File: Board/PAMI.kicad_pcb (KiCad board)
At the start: 4 copper layers, 28.6 x 38.2 mm, 48 parts, among them J1 Conn_01x04_Pin, SW1 Conn_01x03_Pin, U1 BD9P135MUF-CE2, U2 STM32L031F6Px, U3 TC78H621FNG

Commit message: Fix some minor glith on plan & add logo
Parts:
- added G***: LOGO, PAMI:krabi, F.Cu at (71.0, 94.0)

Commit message: Fix DCR
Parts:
- moved SW1 0.31 mm to (84.2, 68.7)
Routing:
- net 9V: track 33.7 -> 33.1 mm

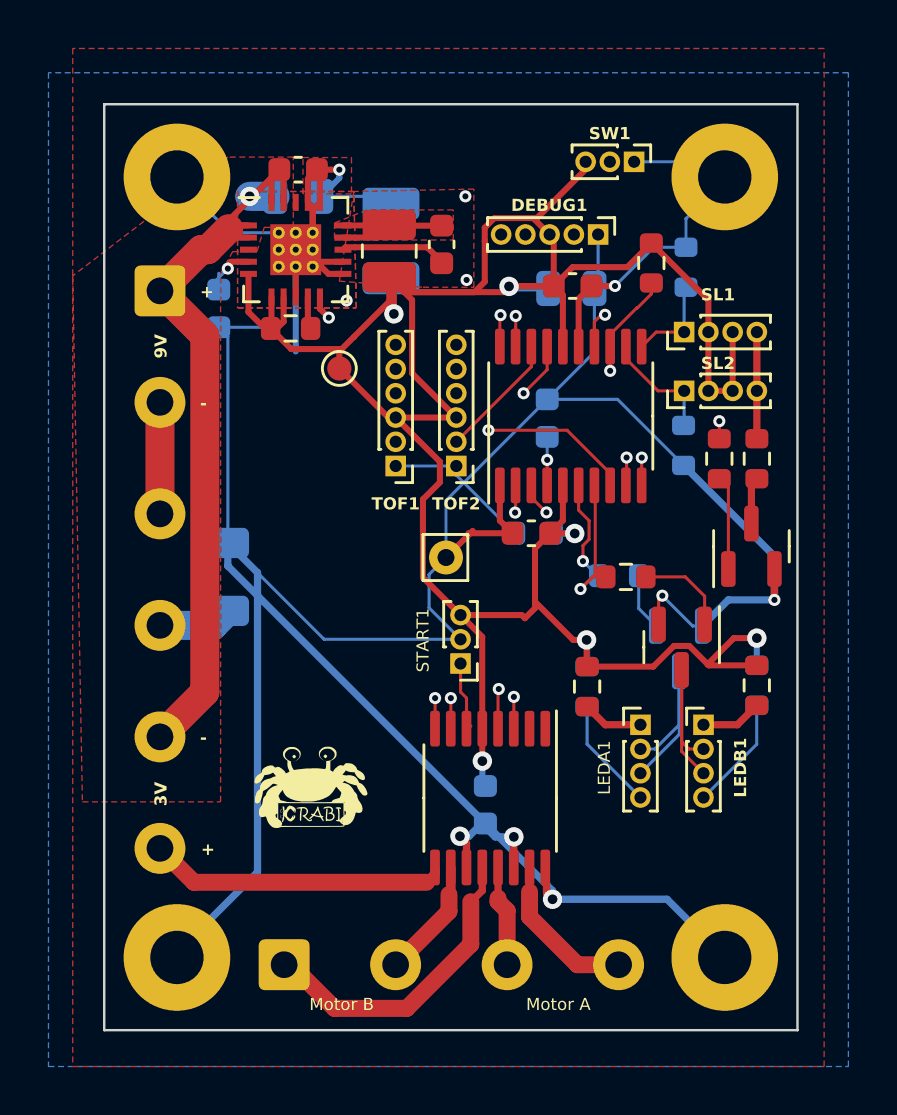
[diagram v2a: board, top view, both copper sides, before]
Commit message: review (fix warnings + GND copper fill on internal layers)
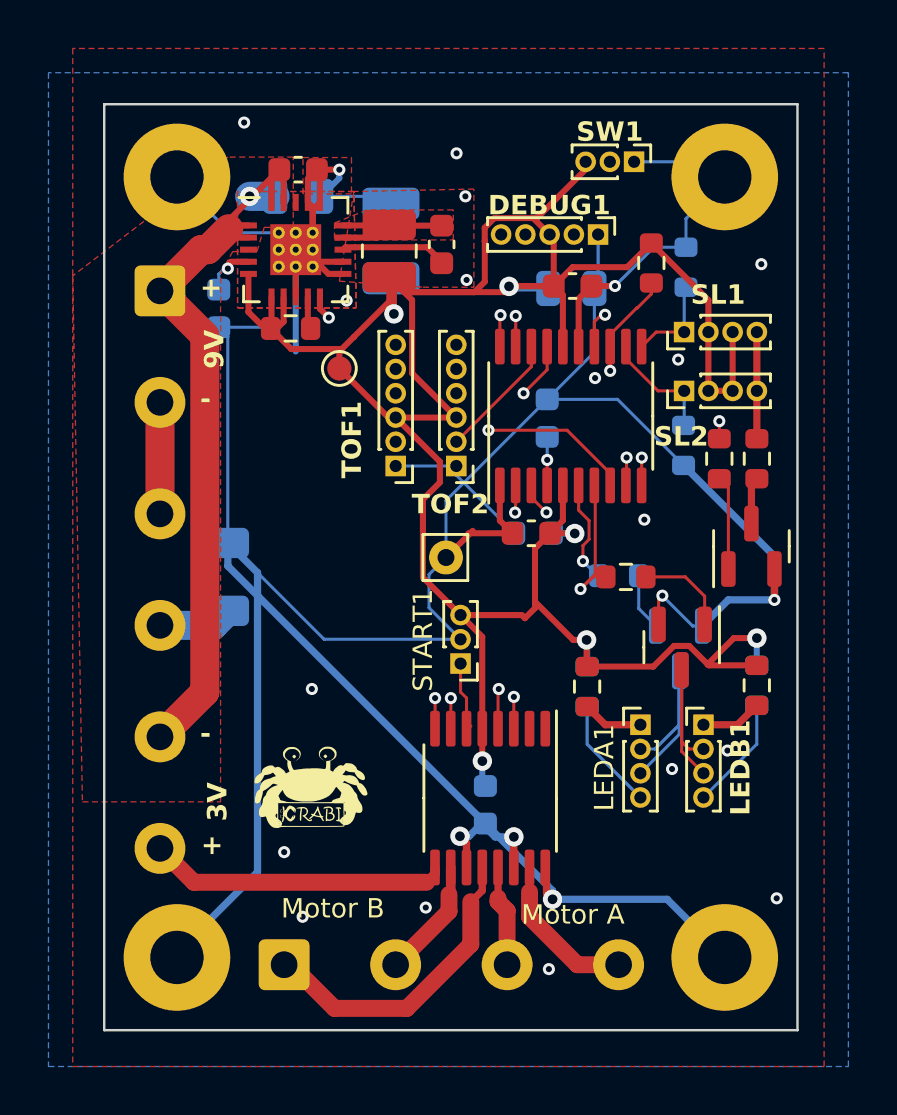
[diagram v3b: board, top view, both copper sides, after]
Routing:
- net GND: vias 10 -> 24
- added copper zone on In1.Cu, net GND
- added copper zone on In2.Cu, net GND
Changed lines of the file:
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@@
     (attr through_hole)
     (fp_text reference "LEDA1" (at -1.491564 1.769999 90) (layer "F.SilkS")
-        (effects (font (size 0.5 0.5) (thickness 0.1)))
+        (effects (font (size 0.8 0.8) (thickness 0.1)))
     )
     (fp_text value "Conn_01x04_Pin" (at -2.9 4.56) (layer "F.Fab")
@@
     (property "ki_keywords" "connector")
     (attr through_hole)
-    (fp_text reference "TOF1" (at 0 -1.56) (layer "F.SilkS")
-        (effects (font (size 0.5 0.5) (thickness 0.1) bold))
+    (fp_text reference "TOF1" (at 1.808 1.088 90) (layer "F.SilkS")
+        (effects (font (size 0.8 0.8) (thickness 0.1) bold))
     )
     (fp_text value "Conn_01x05_Pin" (at -0.1 6.381564) (layer "F.Fab")
@@
     (property "ki_keywords" "connector")
     (attr through_hole)
-    (fp_text reference "SL2" (at 1.135 1.395 180) (layer "F.SilkS")
-        (effects (font (size 0.5 0.5) (thickness 0.1) bold))
+    (fp_text reference "SL2" (at -1.885 -0.119 180) (layer "F.SilkS")
+        (effects (font (size 0.8 0.8) (thickness 0.1) bold))
     )
     (fp_text value "Conn_01x04_Pin" (at 0 4.56 90) (layer "F.Fab")
@@
     (attr through_hole)
     (fp_text reference "START1" (at 1.55 0.965 270) (layer "F.SilkS")
-        (effects (font (size 0.5 0.5) (thickness 0.1)))
+        (effects (font (size 0.8 0.8) (thickness 0.1)))
     )
     (fp_text value "Conn_01x03_Pin" (at 0 3.56) (layer "F.Fab")
@@
     (attr through_hole)
     (fp_text reference "SL1" (at 1.54 1.395) (layer "F.SilkS")
-        (effects (font (size 0.5 0.5) (thickness 0.1) bold))
+        (effects (font (size 0.8 0.8) (thickness 0.1) bold))
     )
     (fp_text value "Conn_01x04_Pin" (at 0 4.56 90) (layer "F.Fab")
@@
     (property "ki_keywords" "connector")
     (attr through_hole)
-    (fp_text reference "SW1" (at -1.165 1.005) (layer "F.SilkS")
-        (effects (font (size 0.5 0.5) (thickness 0.1) bold))
+    (fp_text reference "SW1" (at -1.238 1.005) (layer "F.SilkS")
+        (effects (font (size 0.8 0.8) (thickness 0.1) bold))
     )
     (fp_text value "Conn_01x03_Pin" (at 0 3.56 90) (layer "F.Fab")
@@
     (at 71 94)
     (attr board_only exclude_from_pos_files exclude_from_bom)
-    (fp_text reference "G***" (at -0.4 -2.3) (layer "F.Fab")
+    (fp_text reference "G***" (at -0.4 -2.3) (layer "F.Fab") hide
         (effects (font (size 1.5 1.5) (thickness 0.3)))
     )
@@
     (attr through_hole)
     (fp_text reference "LEDB1" (at 1.528436 1.77 90) (layer "F.SilkS")
-        (effects (font (size 0.5 0.5) (thickness 0.1) bold))
+        (effects (font (size 0.8 0.8) (thickness 0.1) bold))
     )
     (fp_text value "Conn_01x04_Pin" (at 0 4.56) (layer "F.Fab")
@@
     (property "ki_keywords" "connector")
     (attr through_hole)
-    (fp_text reference "TOF2" (at 0 -1.56) (layer "F.SilkS")
-        (effects (font (size 0.5 0.5) (thickness 0.1) bold))
+    (fp_text reference "TOF2" (at 0.244 -1.579) (layer "F.SilkS")
+        (effects (font (size 0.8 0.8) (thickness 0.1) bold))
     )
     (fp_text value "Conn_01x05_Pin" (at -5.425 6.581564) (layer "F.Fab")
@@
     (attr through_hole)
     (fp_text reference "DEBUG1" (at -1.205 2.015) (layer "F.SilkS")
-        (effects (font (size 0.5 0.5) (thickness 0.1) bold))
+        (effects (font (size 0.8 0.8) (thickness 0.1) bold))
     )
     (fp_text value "Conn_01x05_Pin" (at -0.3 7.16 90) (layer "F.Fab")
@@
   (gr_rect (start 62.3 66.3) (end 90.9 104.5)
     (stroke (width 0.1) (type default)) (fill none) (layer "Edge.Cuts"))
-  (gr_text "3V" (at 64.932 95.26 90) (layer "F.SilkS")
-    (effects (font (size 0.5 0.5) (thickness 0.1) bold) (justify left bottom))
+  (gr_text "3V" (at 67.437 95.885 90) (layer "F.SilkS")
+    (effects (font (size 0.8 0.8) (thickness 0.1) bold) (justify left bottom))
   )
   (gr_text "+" (at 66.25 74.332) (layer "F.SilkS")
-    (effects (font (size 0.5 0.5) (thickness 0.1) bold) (justify left bottom))
+    (effects (font (size 0.8 0.8) (thickness 0.1) bold) (justify left bottom))
   )
-  (gr_text "Motor B" (at 70.76 103.73) (layer "F.SilkS")
-    (effects (font (size 0.5 0.5) (thickness 0.1)) (justify left bottom))
+  (gr_text "Motor B" (at 69.596 99.949) (layer "F.SilkS")
+    (effects (font (size 0.8 0.8) (thickness 0.1)) (justify left bottom))
   )
   (gr_text "-" (at 66.25 92.732) (layer "F.SilkS")
-    (effects (font (size 0.5 0.5) (thickness 0.1) bold) (justify left bottom))
+    (effects (font (size 0.8 0.8) (thickness 0.1) bold) (justify left bottom))
   )
   (gr_text "-" (at 66.25 78.932) (layer "F.SilkS")
-    (effects (font (size 0.5 0.5) (thickness 0.1) bold) (justify left bottom))
+    (effects (font (size 0.8 0.8) (thickness 0.1) bold) (justify left bottom))
   )
-  (gr_text "Motor A" (at 79.7 103.73) (layer "F.SilkS")
-    (effects (font (size 0.5 0.5) (thickness 0.1)) (justify left bottom))
+  (gr_text "Motor A" (at 79.502 100.203) (layer "F.SilkS")
+    (effects (font (size 0.8 0.8) (thickness 0.1)) (justify left bottom))
   )
-  (gr_text "9V" (at 64.932 76.79 90) (layer "F.SilkS")
-    (effects (font (size 0.5 0.5) (thickness 0.1) bold) (justify left bottom))
+  (gr_text "9V" (at 67.31 77.216 90) (layer "F.SilkS")
+    (effects (font (size 0.8 0.8) (thickness 0.1) bold) (justify left bottom))
   )
   (gr_text "+" (at 66.29 97.332) (layer "F.SilkS")
-    (effects (font (size 0.5 0.5) (thickness 0.1) bold) (justify left bottom))
+    (effects (font (size 0.8 0.8) (thickness 0.1) bold) (justify left bottom))
   )
   (segment (start 79.146564 84) (end 77.321564 84) (width 0.25) (layer "F.Cu") (net 1))
@@
   (via (at 72.3 74.4) (size 0.5) (drill 0.25) (layers "F.Cu" "B.Cu") (free) (net 1))
   (via (at 80.796064 99.1) (size 0.8) (drill 0.4) (layers "F.Cu" "B.Cu") (net 1))
+  (via (at 75.565 99.441) (size 0.5) (drill 0.25) (layers "F.Cu" "B.Cu") (free) (net 1))
+  (via (at 70.485 99.822) (size 0.5) (drill 0.25) (layers "F.Cu" "B.Cu") (free) (net 1))
+  (via (at 88.011 92.964) (size 0.5) (drill 0.25) (layers "F.Cu" "B.Cu") (free) (net 1))
+  (via (at 89.408 72.898) (size 0.5) (drill 0.25) (layers "F.Cu" "B.Cu") (free) (net 1))
+  (via (at 76.835 68.326) (size 0.5) (drill 0.25) (layers "F.Cu" "B.Cu") (free) (net 1))
   (via (at 79.2 96.525) (size 0.8) (drill 0.4) (layers "F.Cu" "B.Cu") (net 1))
   (via (at 85.325 86.575) (size 0.5) (drill 0.25) (layers "F.Cu" "B.Cu") (net 1))
@@
   (via (at 83.371564 73.8) (size 0.5) (drill 0.25) (layers "F.Cu" "B.Cu") (net 1))
   (via (at 72 69) (size 0.5) (drill 0.25) (layers "F.Cu" "B.Cu") (net 1))
+  (via (at 85.979 76.835) (size 0.5) (drill 0.25) (layers "F.Cu" "B.Cu") (free) (net 1))
+  (via (at 82.55 77.597) (size 0.5) (drill 0.25) (layers "F.Cu" "B.Cu") (free) (net 1))
+  (via (at 70.866 90.424) (size 0.5) (drill 0.25) (layers "F.Cu" "B.Cu") (free) (net 1))
   (via (at 89.95 86.75) (size 0.5) (drill 0.25) (layers "F.Cu" "B.Cu") (net 1))
   (via (at 77.25 73.55) (size 0.5) (drill 0.25) (layers "F.Cu" "B.Cu") (free) (net 1))
+  (via (at 90.043 99.06) (size 0.5) (drill 0.25) (layers "F.Cu" "B.Cu") (free) (net 1))
+  (via (at 68.072 67.056) (size 0.5) (drill 0.25) (layers "F.Cu" "B.Cu") (free) (net 1))
   (via (at 76.975 96.5) (size 0.8) (drill 0.4) (layers "F.Cu" "B.Cu") (net 1))
+  (via (at 69.723 97.155) (size 0.5) (drill 0.25) (layers "F.Cu" "B.Cu") (free) (net 1))
+  (via (at 85.725 93.726) (size 0.5) (drill 0.25) (layers "F.Cu" "B.Cu") (free) (net 1))
+  (via (at 80.645 101.981) (size 0.5) (drill 0.25) (layers "F.Cu" "B.Cu") (free) (net 1))
+  (via (at 84.582 83.439) (size 0.5) (drill 0.25) (layers "F.Cu" "B.Cu") (free) (net 1))
   (segment (start 80.575 78.475) (end 82.521564 76.528436) (width 0.1271) (layer "B.Cu") (net 1))
   (segment (start 76.975 96.5) (end 77.35 96.5) (width 0.3) (layer "B.Cu") (net 1))
@@
   (segment (start 69.804489 75.104489) (end 67.5 72.8) (width 0.25) (layer "In1.Cu") (net 6))
   (segment (start 71.565812 75.104489) (end 69.804489 75.104489) (width 0.25) (layer "In1.Cu") (net 6))
-  (segment (start 66.925 73.555) (end 67.4 73.08) (width 0.1271) (layer "B.Cu") (net 6))
-  (segment (start 67.025 73.95) (end 67.025 73.275) (width 0.1271) (layer "B.Cu") (net 6))
+  (segment (start 67.255 73.08) (end 67.4 73.08) (width 0.1271) (layer "B.Cu") (net 6))
+  (segment (start 67.025 73.31) (end 67.255 73.08) (width 0.1271) (layer "B.Cu") (net 6))
+  (segment (start 67.025 73.95) (end 67.025 73.31) (width 0.1271) (layer "B.Cu") (net 6))
   (segment (start 72.25 72.2) (end 72.15 72.3) (width 0.25) (layer "F.Cu") (net 7))
   (segment (start 75.625 72.2) (end 72.25 72.2) (width 0.25) (layer "F.Cu") (net 7))
@@
     )
   )
-  (zone (net 1) (net_name "GND") (layer "B.Cu") (hatch edge 0.5)
+  (zone (net 1) (net_name "GND") (layers "In1.Cu" "In2.Cu" "B.Cu") (hatch edge 0.5)
     (priority 4)
     (connect_pads yes (clearance 0.1271))
